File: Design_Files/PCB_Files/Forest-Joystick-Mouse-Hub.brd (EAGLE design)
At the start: 100 x 40 mm, 24 parts, among them J1 E5566-Q0LK22-L

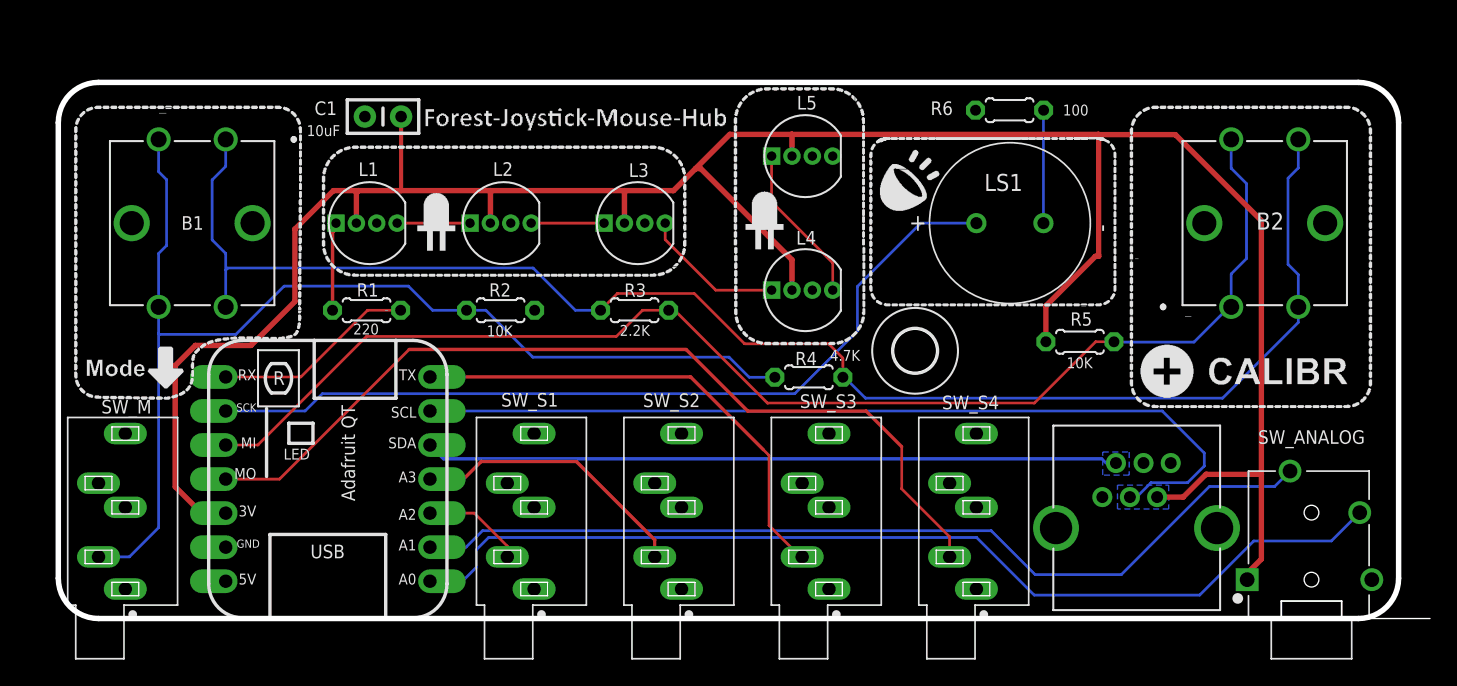
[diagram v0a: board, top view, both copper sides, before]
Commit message: Update resistor size
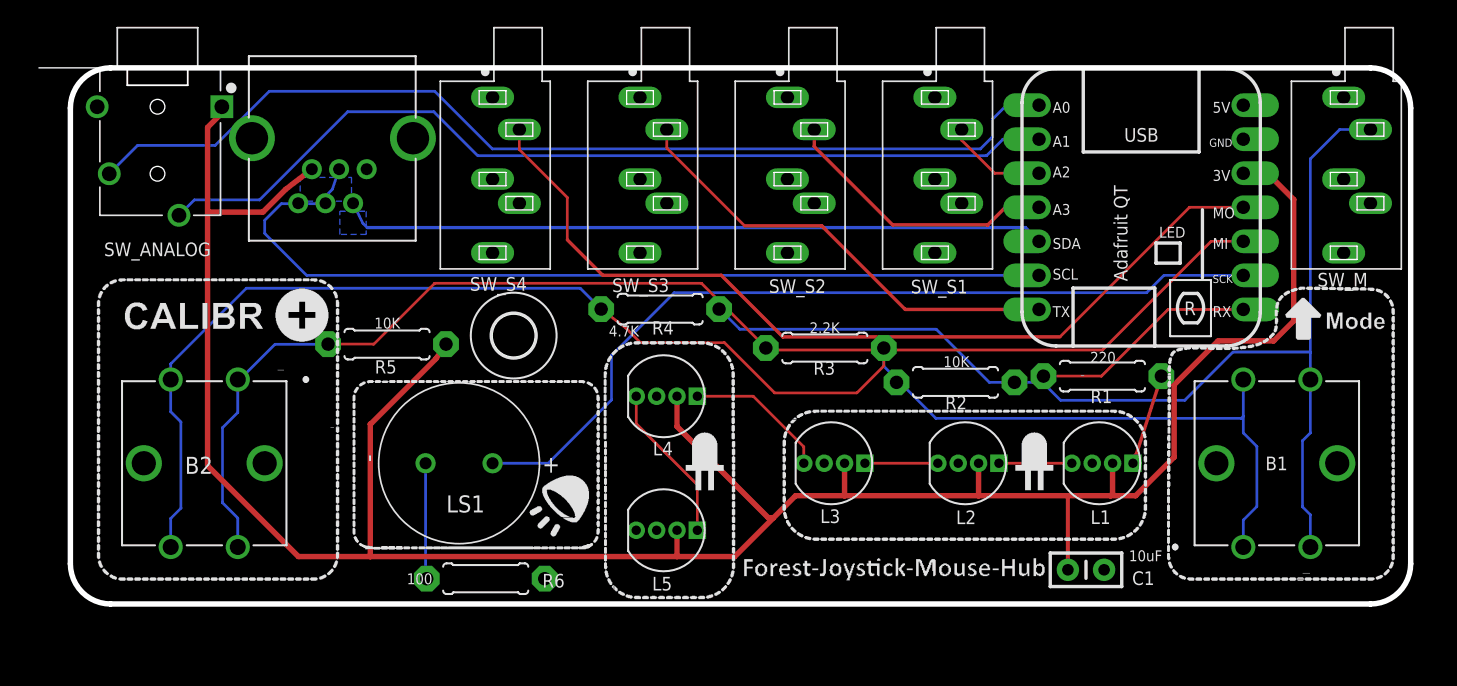
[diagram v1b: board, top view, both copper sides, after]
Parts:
- R1, R2, R3, R4, R5, R6: device MMC Eagle:RESISTOR_0204/5 -> MMC Eagle:RESISTOR_0206/8
- moved SW_M 98.0 mm to (95.9, 38.9), turned to 270 degrees
- moved SW_ANALOG 91.2 mm to (7.40, 35.6), turned to 270 degrees
- moved B1 82.9 mm to (90.9, 11.6), turned to 90 degrees
- moved B2 81.1 mm to (10.9, 11.6), turned to 270 degrees
- moved J1 67.9 mm to (17.9, 31.0), turned to 0 degrees
- moved C1 62.4 mm to (76.7, 3.63), turned to 0 degrees
- moved L1 57.8 mm to (77.9, 11.6), turned to 0 degrees
- moved R1 55.1 mm to (77.9, 18.1), turned to 0 degrees
- moved R6 52.4 mm to (31.9, 2.97), turned to 180 degrees
- moved R5 51.7 mm to (24.5, 20.5), turned to 0 degrees
- moved SW_S4 51.5 mm to (32.4, 38.9), turned to 270 degrees
- moved SW_S1 47.3 mm to (65.4, 38.9), turned to 270 degrees
- moved LS1 44.8 mm to (29.9, 11.6), turned to 180 degrees
- moved MCU 42.9 mm to (71.9, 20.3), turned to 0 degrees
- moved SW_S3 39.3 mm to (43.4, 38.9), turned to 270 degrees
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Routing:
- net N$1: track 115.9 -> 118.3 mm
- net PIN_SW_S3: track 36.4 -> 34.1 mm
- net +3V3: track 187.4 -> 189.4 mm
- net PIN_LEDS: track 15.1 -> 17.0 mm
- net N$5: track 85.1 -> 83.3 mm
- net PIN_BUTTON: track 98.5 -> 96.9 mm
- net PIN_SCL: track 66.5 -> 67.6 mm
- net PIN_SDA: track 51.7 -> 52.7 mm

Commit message: PCB Updates
 - Footprint for larger resistors
 - Added OSHWA Certification logo
 - Updated Gerbers
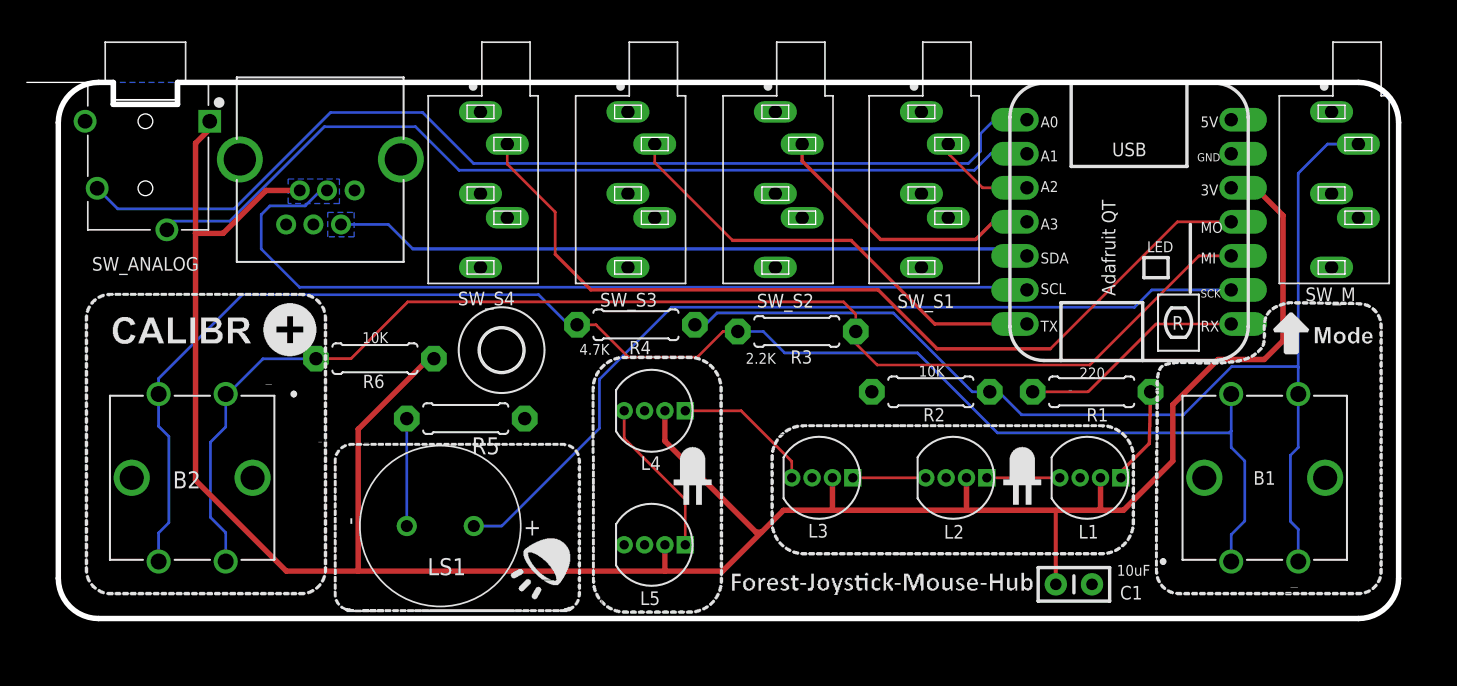
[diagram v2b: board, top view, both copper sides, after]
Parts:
- added LOGO-OSHWA: CA000033, MMC Eagle:OSHWA-CERT-SMALL-SILK
- R5: value 10K -> 100
- R6: value 100 -> 10K
- moved R6 18.4 mm to (23.6, 19.4), turned to 0 degrees
- moved R5 8.08 mm to (30.4, 14.9), turned to 180 degrees
- moved LS1 4.89 mm to (28.5, 6.90)
- moved R3 2.43 mm to (55.1, 21.4), turned to 0 degrees
- moved R4 2.15 mm to (43.1, 21.9)
- moved R2 1.97 mm to (65.1, 16.9)
- moved J1 1.82 mm to (17.0, 29.4)
- moved SW_S1 1.48 mm to (64.4, 37.8)
- moved R1 1.42 mm to (77.1, 16.9)
- moved SW_M 1.41 mm to (95.0, 37.8)
- moved SW_S2 1.41 mm to (53.5, 37.8)
- moved SW_S3 1.41 mm to (42.5, 37.8)
- moved SW_S4 1.41 mm to (31.5, 37.8)
- moved B2 1.41 mm to (10.0, 10.5)
- moved H1 1.41 mm to (33.1, 20.0)
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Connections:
- net +3V3: now also R6.2; no longer R5.2
- net GND: now also R5.1; no longer R6.1
- net N$12: now also R5.2; no longer R6.2
- net PIN_BUTTON: now also R6.1; no longer R5.1
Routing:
- net PIN_BUZZER: track 63.8 -> 66.0 mm
- net N$1: track 118.3 -> 116.2 mm
- net N$5: track 83.3 -> 84.9 mm
- net PIN_SCL: track 67.6 -> 66.6 mm
- net PIN_BUTTON: track 96.9 -> 97.9 mm
- net PIN_A0: track 75.8 -> 76.7 mm
- net N$12: track 8.70 -> 8.02 mm
- net PIN_SDA: track 52.7 -> 52.2 mm
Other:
- outline, holes or cut-outs redrawn
- board text added: "https://github.com/makersmakingchange/Forest-Joystick-Mouse-Hub"
- board text removed: "www.makersmakingchange.com"
